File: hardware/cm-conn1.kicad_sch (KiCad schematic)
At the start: 7 parts, among them J3 RJ45_RB1-125B8G1A

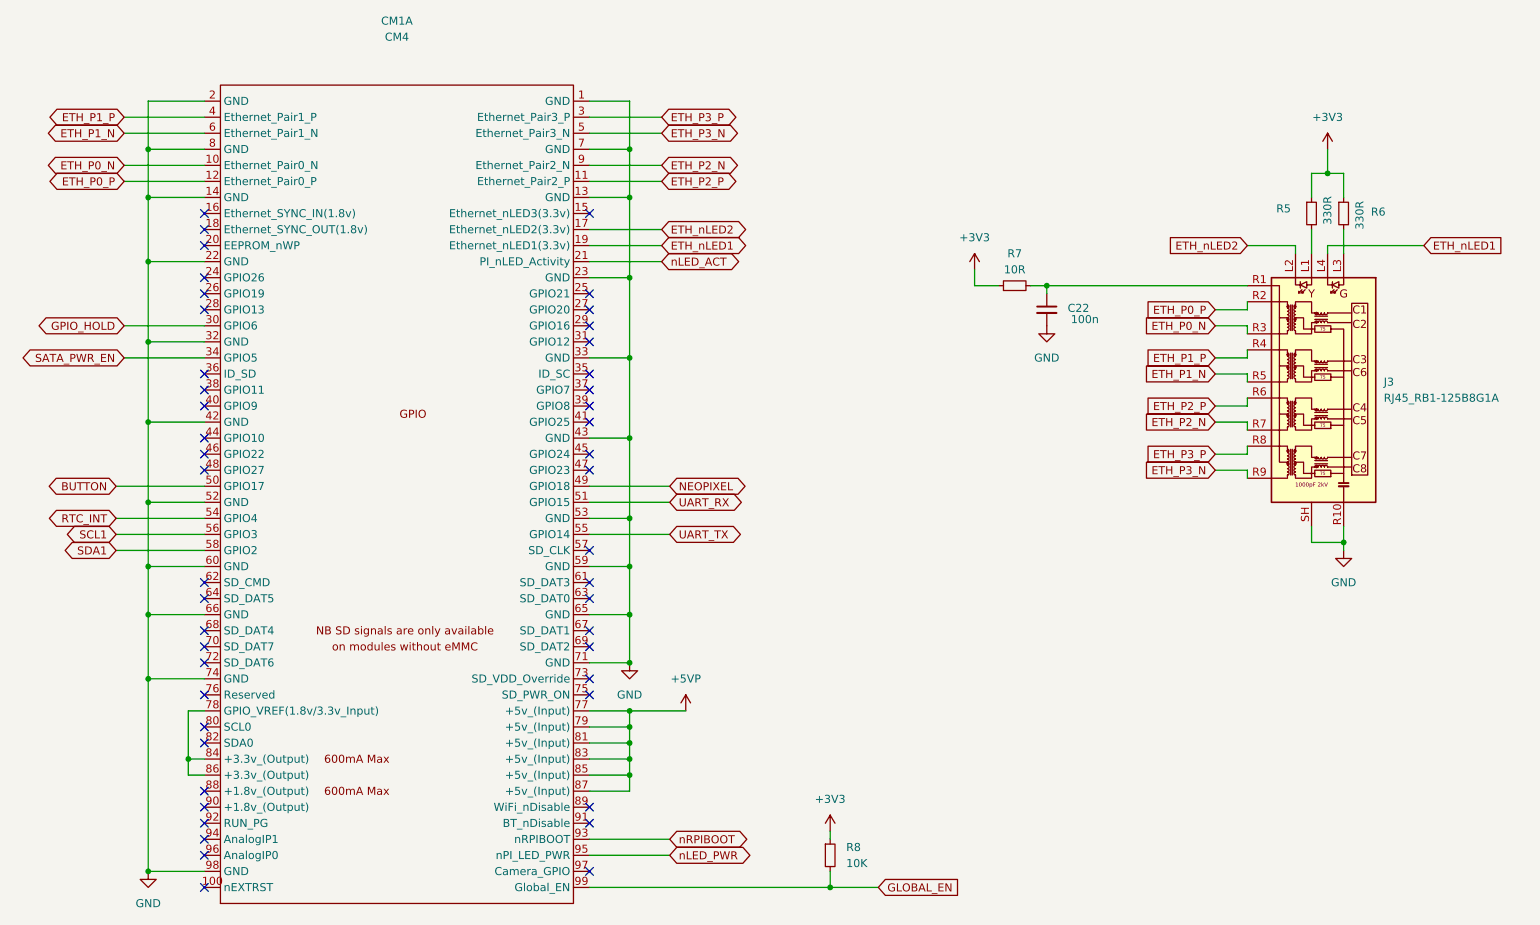
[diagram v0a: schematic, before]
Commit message: refactor: reannotate PCB by position + rename IC1 to U prefix
All reference designators renumbered top-to-bottom, left-to-right.
ASM1061 changed from IC to U prefix.
ERC: 0 errors. DRC: 0 violations. Parity: 0 issues.
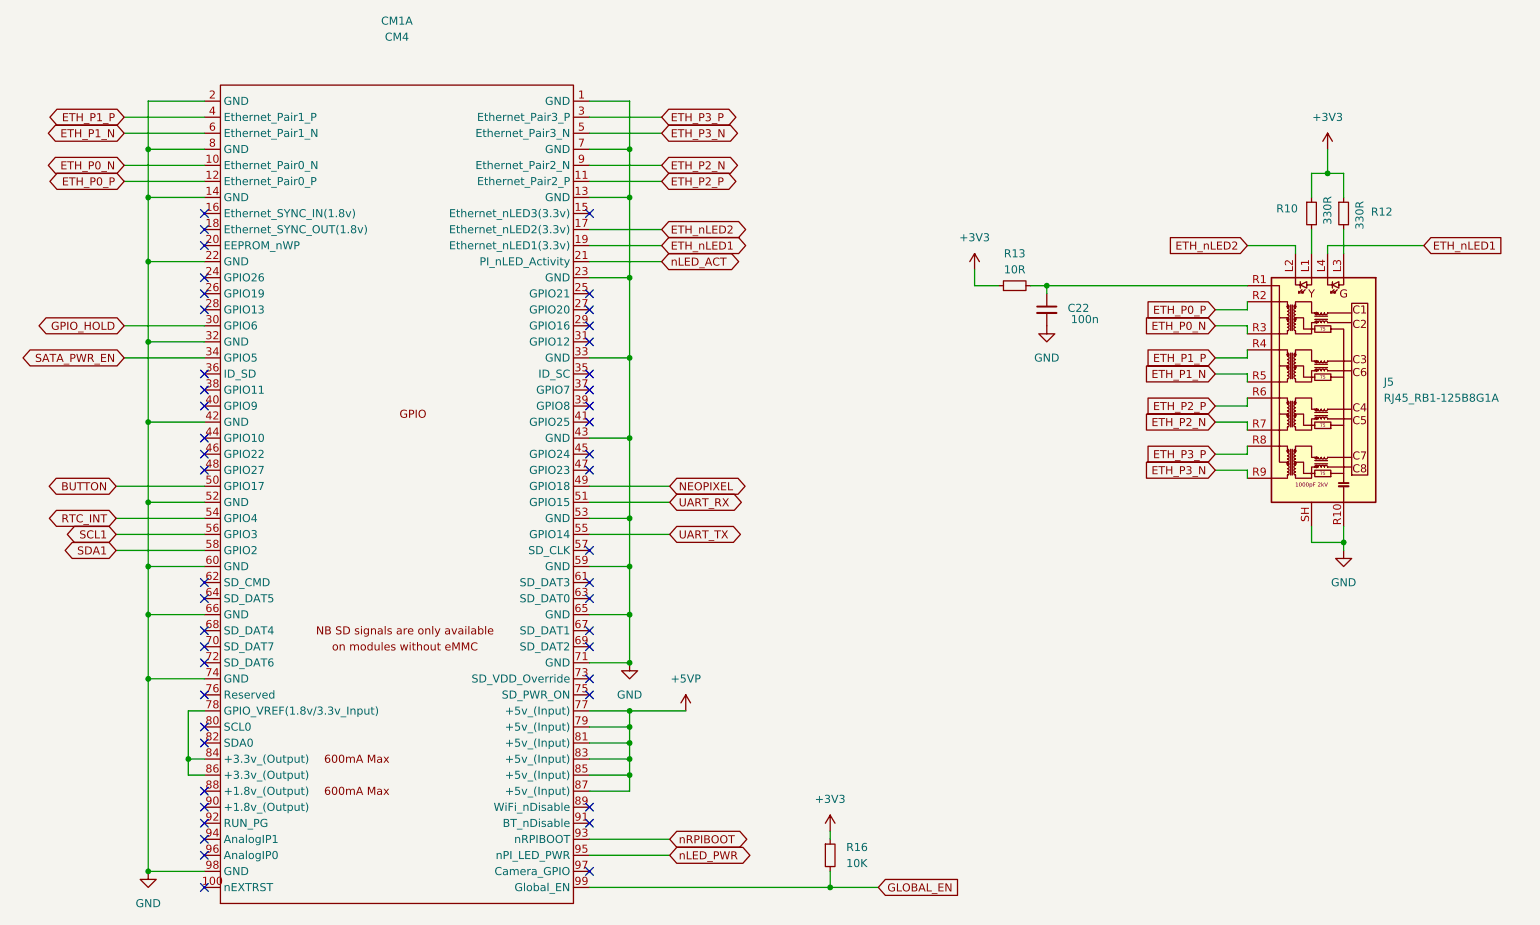
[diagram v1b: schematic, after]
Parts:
- C22: KiLib_Generator (none) -> SMD_2terminal_chip_molded
- R10: renamed from R5; KiLib_Generator (none) -> SMD_2terminal_chip_molded
- R12: renamed from R6; KiLib_Generator (none) -> SMD_2terminal_chip_molded
- R13: renamed from R7; KiLib_Generator (none) -> SMD_2terminal_chip_molded
- R16: renamed from R8; KiLib_Generator (none) -> SMD_2terminal_chip_molded
- renumbered J3 to J5
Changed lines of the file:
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@@
+			)
+		)
+		(property "KiLib_Generator" "SMD_2terminal_chip_molded"
+			(at 187.96 73.66 0)
+			(hide yes)
+			(show_name no)
+			(do_not_autoplace no)
+			(effects
+				(font
+					(size 1.27 1.27)
+				)
 			)
 		)
@@
 		(in_pos_files yes)
 		(dnp no)
-		(property "Reference" "J3"
+		(property "Reference" "J5"
 			(at 241.3 85.0899 0)
 			(show_name no)
@@
 			(project "granit"
 				(path "/d2c135e3-a983-4cd4-8cff-b50ca3c7671a/425bdf56-ee3a-43f6-b6d9-8fa9cc85dc16"
-					(reference "J3")
+					(reference "J5")
 					(unit 1)
 				)
@@
 		(dnp no)
 		(fields_autoplaced yes)
-		(property "Reference" "R7"
+		(property "Reference" "R13"
 			(at 182.88 64.77 90)
 			(show_name no)
@@
 		)
 		(property "Description" "Resistor, small symbol"
+			(at 182.88 69.85 0)
+			(hide yes)
+			(show_name no)
+			(do_not_autoplace no)
+			(effects
+				(font
+					(size 1.27 1.27)
+				)
+			)
+		)
+		(property "KiLib_Generator" "SMD_2terminal_chip_molded"
 			(at 182.88 69.85 0)
 			(hide yes)
@@
 			(project "granit"
 				(path "/d2c135e3-a983-4cd4-8cff-b50ca3c7671a/425bdf56-ee3a-43f6-b6d9-8fa9cc85dc16"
-					(reference "R7")
+					(reference "R13")
 					(unit 1)
 				)
@@
 		(dnp no)
 		(fields_autoplaced yes)
-		(property "Reference" "R8"
+		(property "Reference" "R16"
 			(at 156.21 158.7499 0)
 			(show_name no)
@@
 		)
 		(property "Description" "Resistor, small symbol"
+			(at 153.67 160.02 0)
+			(hide yes)
+			(show_name no)
+			(do_not_autoplace no)
+			(effects
+				(font
+					(size 1.27 1.27)
+				)
+			)
+		)
+		(property "KiLib_Generator" "SMD_2terminal_chip_molded"
 			(at 153.67 160.02 0)
 			(hide yes)
@@
 			(project "granit"
 				(path "/d2c135e3-a983-4cd4-8cff-b50ca3c7671a/425bdf56-ee3a-43f6-b6d9-8fa9cc85dc16"
-					(reference "R8")
+					(reference "R16")
 					(unit 1)
 				)
@@
 		(in_pos_files yes)
 		(dnp no)
-		(property "Reference" "R6"
+		(property "Reference" "R12"
 			(at 239.268 58.166 0)
 			(show_name no)
@@
 		)
 		(property "Description" "Resistor, small symbol"
+			(at 234.95 58.42 0)
+			(hide yes)
+			(show_name no)
+			(do_not_autoplace no)
+			(effects
+				(font
+					(size 1.27 1.27)
+				)
+			)
+		)
+		(property "KiLib_Generator" "SMD_2terminal_chip_molded"
 			(at 234.95 58.42 0)
 			(hide yes)
@@
 			(project "granit"
 				(path "/d2c135e3-a983-4cd4-8cff-b50ca3c7671a/425bdf56-ee3a-43f6-b6d9-8fa9cc85dc16"
-					(reference "R6")
+					(reference "R12")
 					(unit 1)
 				)
@@
 		(in_pos_files yes)
 		(dnp no)
-		(property "Reference" "R5"
+		(property "Reference" "R10"
 			(at 224.282 57.658 0)
 			(show_name no)
@@
 		)
 		(property "Description" "Resistor, small symbol"
+			(at 229.87 58.42 0)
+			(hide yes)
+			(show_name no)
+			(do_not_autoplace no)
+			(effects
+				(font
+					(size 1.27 1.27)
+				)
+			)
+		)
+		(property "KiLib_Generator" "SMD_2terminal_chip_molded"
 			(at 229.87 58.42 0)
 			(hide yes)
@@
 			(project "granit"
 				(path "/d2c135e3-a983-4cd4-8cff-b50ca3c7671a/425bdf56-ee3a-43f6-b6d9-8fa9cc85dc16"
-					(reference "R5")
+					(reference "R10")
 					(unit 1)
 				)
